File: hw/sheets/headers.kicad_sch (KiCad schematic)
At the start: 17 parts, among them J20 HDR_J20, J21 HDR_J21, J22 HDR_J22, J23 HDR_J23, J24 HDR_J24, J25 HDR_J25, J26 HDR_J26, J27 HDR_J27, J28 HDR_J28, J29 HDR_J29, J30 HDR_J30, J31 HDR_J31, J32 HDR_J32, J33 HDR_J33, J34 HDR_J34, J35 HDR_J35, J36 HDR_J36

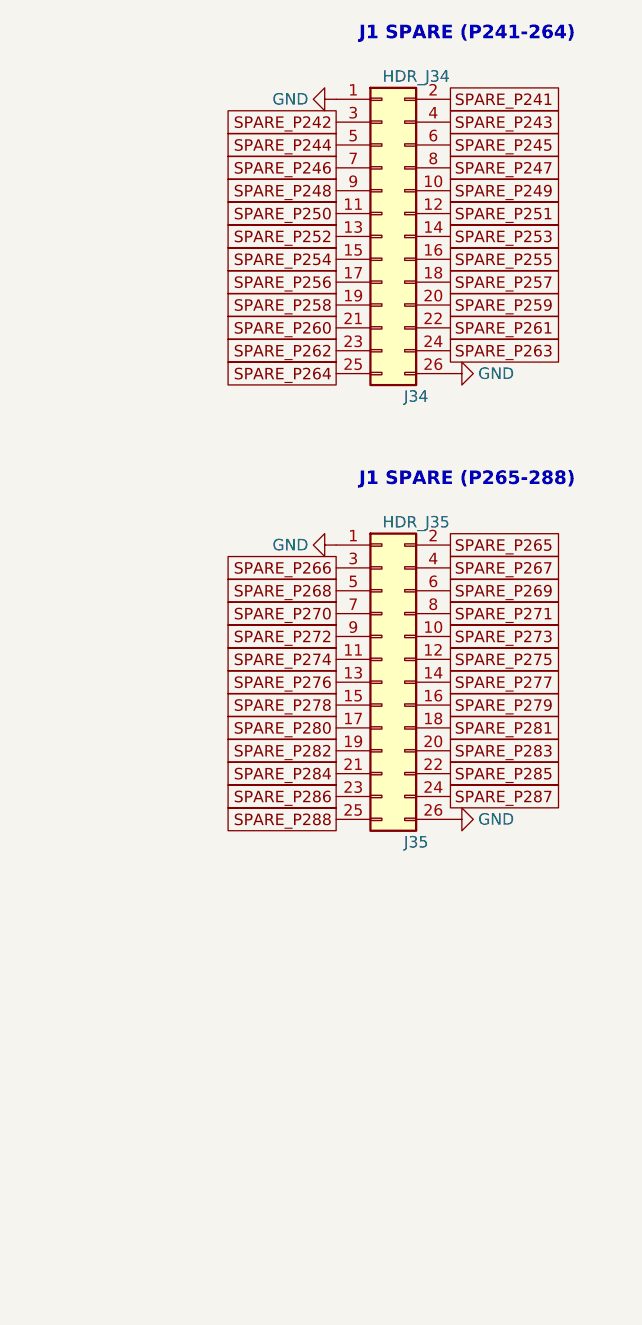
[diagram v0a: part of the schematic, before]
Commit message: Add MSC1 breakout (J37), ground J35 spare pads, add audio amp/mic tap (J38)
Carve J35's last 6 pins into a new MSC1 header (J37: CLK/CMD/D0-D3_CD),
keeping J35 at a fixed 26-pin size in both schematic and PCB with the
now-orphaned pads tied to GND. Add a 3-pin tap (J38) off the audio jack
(HPOUTL/GND/MICLP) so an external amplifier or mic can be wired in
directly instead of needing a breakout cable off J6.
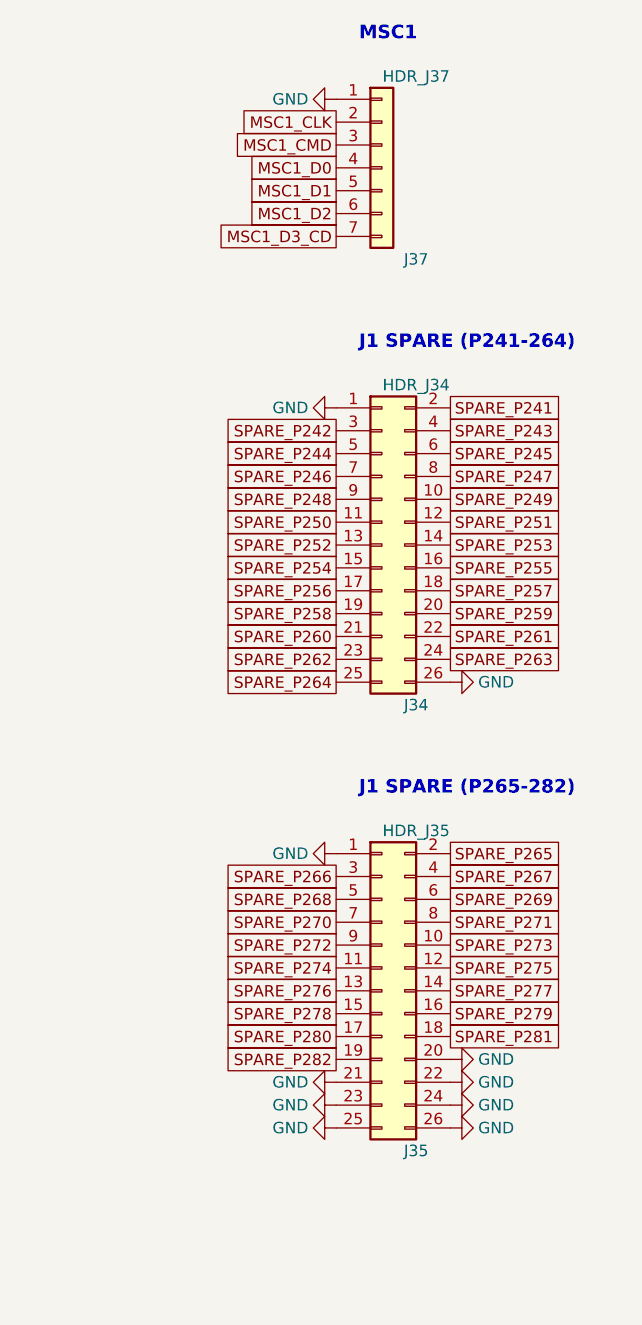
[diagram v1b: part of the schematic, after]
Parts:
- added J37: HDR_J37, Connector_PinHeader_2.54mm:PinHeader_1x07_P2.54mm_Vertical, symbol Connector_Generic:Conn_01x07
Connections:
- net SPARE_P283 is gone; now on net GND: J35.20 (Pin_20)
- net SPARE_P284 is gone; now on net GND: J35.21 (Pin_21)
- net SPARE_P285 is gone; now on net GND: J35.22 (Pin_22)
- net SPARE_P286 is gone; now on net GND: J35.23 (Pin_23)
- net SPARE_P287 is gone; now on net GND: J35.24 (Pin_24)
- net SPARE_P288 is gone; now on net GND: J35.25 (Pin_25)
- net GND: now also J37.1 (Pin_1)
- new net MSC1_CLK: J37.2 (Pin_2)
- new net MSC1_CMD: J37.3 (Pin_3)
- new net MSC1_D0: J37.4 (Pin_4)
- new net MSC1_D1: J37.5 (Pin_5)
- new net MSC1_D2: J37.6 (Pin_6)
- new net MSC1_D3_CD: J37.7 (Pin_7)
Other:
- note added: "J1 SPARE (P265-282)"
- note added: "MSC1"
- note removed: "J1 SPARE (P265-288)"
